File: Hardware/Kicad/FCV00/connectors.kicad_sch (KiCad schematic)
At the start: 24 parts, among them J2 ESC, J3 RX, J4 VTX, J5 CAM, J6 GPS, J7 AUX, Q1 2N7002

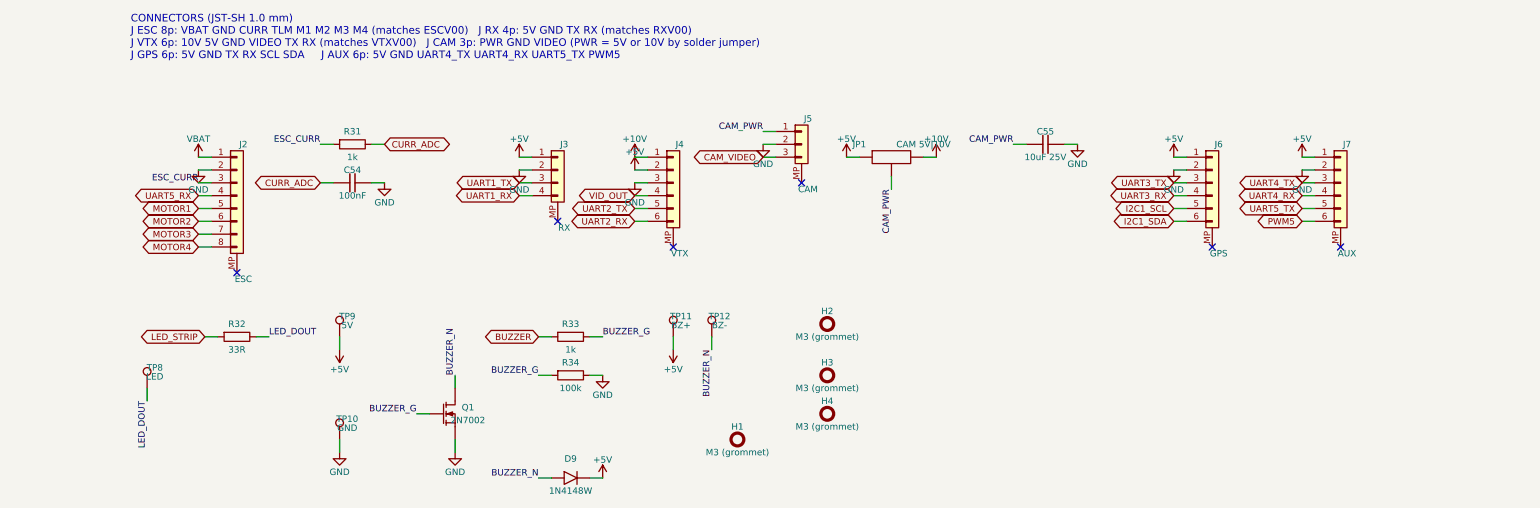
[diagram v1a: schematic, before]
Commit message: Boards follow the B0_EE part convention
- every real part uses the symbol/footprint/3D/datasheet named after its MPN in Kicad_Libs
- symbols keep only Reference, Value, Footprint, Datasheet, Description
  (MPN, Manufacturer, Verify, LCSC, Note fields removed; Verify notes moved to the Readme)
- schematic symbol caches rebuilt from the libraries, PCB footprints relinked with the
  same fields and 3D models as the library (connectivity unchanged)
- DNP and BOM attributes of the footprints match the symbols
- BOMs re-exported with kicad-cli
- ignore KiCad local history
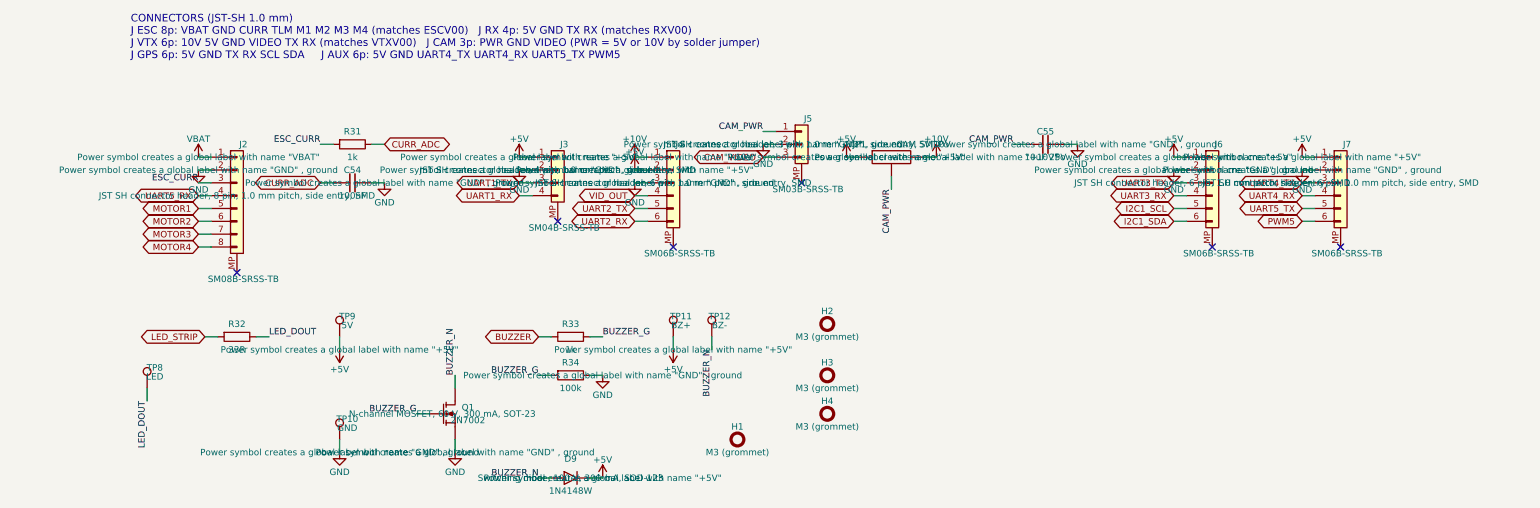
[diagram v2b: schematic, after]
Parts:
- D9: footprint eDiodes:D_SOD-123 -> eDiodes:1N4148W; symbol eDiodes:D -> eDiodes:1N4148W; MPN 1N4148W -> (none)
- H1, H2, H3, H4, JP1, TP10, TP11, TP12, TP8, TP9: now left out of the parts list
- J2: value ESC -> SM08B-SRSS-TB; footprint eConnector:JST_SH_SM08B-SRSS-TB_1x08-1MP_P1.00mm_Horizontal -> eConnector:SM08B-SRSS-TB; symbol eConnector:JST_SH_SM08B-SRSS-TB -> eConnector:SM08B-SRSS-TB; MPN SM08B-SRSS-TB(LF)(SN) -> (none); Manufacturer JST -> (none)
- J3: value RX -> SM04B-SRSS-TB; footprint eConnector:JST_SH_SM04B-SRSS-TB_1x04-1MP_P1.00mm_Horizontal -> eConnector:SM04B-SRSS-TB; symbol eConnector:JST_SH_SM04B-SRSS-TB -> eConnector:SM04B-SRSS-TB; MPN SM04B-SRSS-TB(LF)(SN) -> (none); Manufacturer JST -> (none)
- J4: value VTX -> SM06B-SRSS-TB; footprint eConnector:JST_SH_SM06B-SRSS-TB_1x06-1MP_P1.00mm_Horizontal -> eConnector:SM06B-SRSS-TB; symbol eConnector:JST_SH_SM06B-SRSS-TB -> eConnector:SM06B-SRSS-TB; MPN SM06B-SRSS-TB(LF)(SN) -> (none); Manufacturer JST -> (none)
- J5: value CAM -> SM03B-SRSS-TB; footprint eConnector:JST_SH_SM03B-SRSS-TB_1x03-1MP_P1.00mm_Horizontal -> eConnector:SM03B-SRSS-TB; symbol eConnector:JST_SH_SM03B-SRSS-TB -> eConnector:SM03B-SRSS-TB; MPN SM03B-SRSS-TB(LF)(SN) -> (none); Manufacturer JST -> (none)
- J6: value GPS -> SM06B-SRSS-TB; footprint eConnector:JST_SH_SM06B-SRSS-TB_1x06-1MP_P1.00mm_Horizontal -> eConnector:SM06B-SRSS-TB; symbol eConnector:JST_SH_SM06B-SRSS-TB -> eConnector:SM06B-SRSS-TB; MPN SM06B-SRSS-TB(LF)(SN) -> (none); Manufacturer JST -> (none)
- J7: value AUX -> SM06B-SRSS-TB; footprint eConnector:JST_SH_SM06B-SRSS-TB_1x06-1MP_P1.00mm_Horizontal -> eConnector:SM06B-SRSS-TB; symbol eConnector:JST_SH_SM06B-SRSS-TB -> eConnector:SM06B-SRSS-TB; MPN SM06B-SRSS-TB(LF)(SN) -> (none); Manufacturer JST -> (none)
- Q1: footprint eTransistor:SOT-23 -> eTransistor:2N7002; LCSC C8545 -> (none); MPN 2N7002,215 -> (none); Manufacturer Nexperia -> (none)

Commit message: Cleared all the descriptions and started Power section for FCV
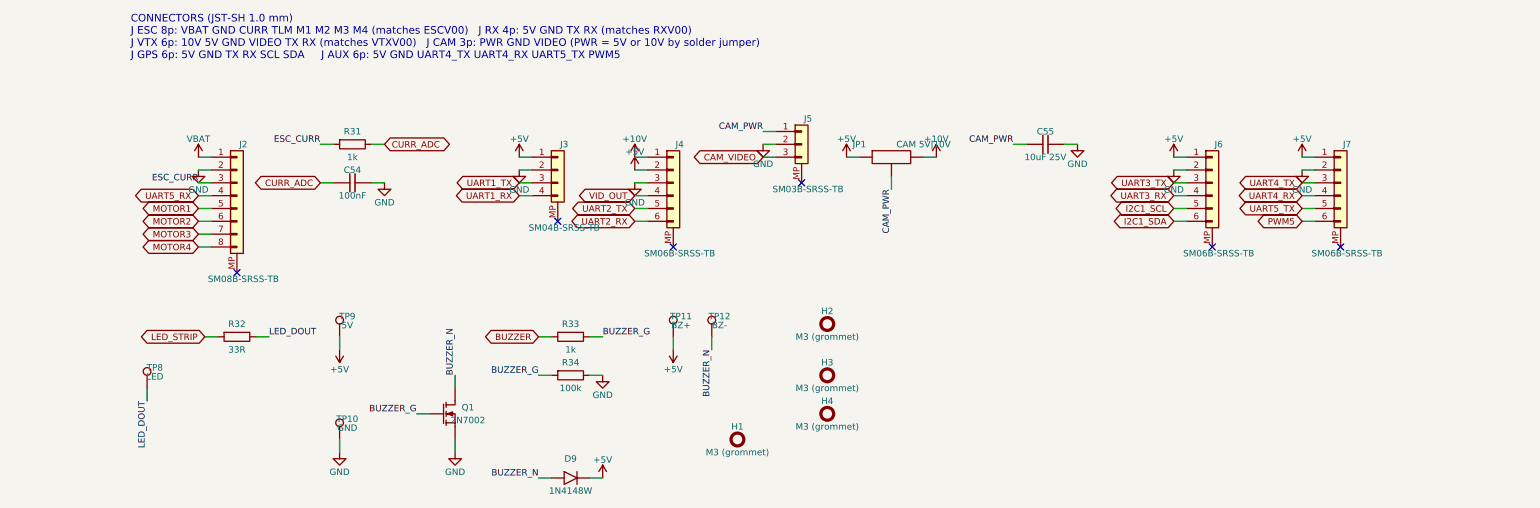
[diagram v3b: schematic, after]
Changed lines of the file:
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@@
 		(property "Description" "Power symbol creates a global label with name \"GND\" , ground"
 			(at 137.16 40.64 0)
+			(hide yes)
 			(show_name no)
 			(do_not_autoplace no)
@@
 		(property "Description" "Power symbol creates a global label with name \"GND\" , ground"
 			(at 111.76 48.26 0)
+			(hide yes)
 			(show_name no)
 			(do_not_autoplace no)
@@
 		(property "Description" "Power symbol creates a global label with name \"+5V\""
 			(at 111.76 45.72 0)
+			(hide yes)
 			(show_name no)
 			(do_not_autoplace no)
@@
 		(property "Description" "Power symbol creates a global label with name \"GND\" , ground"
 			(at 199.39 40.64 0)
+			(hide yes)
 			(show_name no)
 			(do_not_autoplace no)
@@
 		(property "Description" "JST SH connector header, 6 pin, 1.0 mm pitch, side entry, SMD"
 			(at 226.06 48.26 0)
+			(hide yes)
 			(show_name no)
 			(do_not_autoplace no)
@@
 		(property "Description" "Power symbol creates a global label with name \"+5V\""
 			(at 119.38 81.28 0)
+			(hide yes)
 			(show_name no)
 			(do_not_autoplace no)
@@
 		(property "Description" "Power symbol creates a global label with name \"+5V\""
 			(at 153.67 43.18 0)
+			(hide yes)
 			(show_name no)
 			(do_not_autoplace no)
@@
 		(property "Description" "Power symbol creates a global label with name \"+5V\""
 			(at 53.34 81.28 0)
+			(hide yes)
 			(show_name no)
 			(do_not_autoplace no)
@@
 		(property "Description" "Switching diode, 100 V, 300 mA, SOD-123"
 			(at 99.06 106.68 0)
+			(hide yes)
 			(show_name no)
 			(do_not_autoplace no)
@@
 		(property "Description" "Power symbol creates a global label with name \"+5V\""
 			(at 218.44 43.18 0)
+			(hide yes)
 			(show_name no)
 			(do_not_autoplace no)
@@
 		(property "Description" "JST SH connector header, 3 pin, 1.0 mm pitch, side entry, SMD"
 			(at 144.78 40.64 0)
+			(hide yes)
 			(show_name no)
 			(do_not_autoplace no)
@@
 		(property "Description" "Power symbol creates a global label with name \"GND\" , ground"
 			(at 76.2 101.6 0)
+			(hide yes)
 			(show_name no)
 			(do_not_autoplace no)
@@
 		(property "Description" "Power symbol creates a global label with name \"+5V\""
 			(at 88.9 43.18 0)
+			(hide yes)
 			(show_name no)
 			(do_not_autoplace no)
@@
 		(property "Description" "Power symbol creates a global label with name \"+5V\""
 			(at 105.41 106.68 0)
+			(hide yes)
 			(show_name no)
 			(do_not_autoplace no)
@@
 		(property "Description" "Power symbol creates a global label with name \"GND\" , ground"
 			(at 62.23 48.26 0)
+			(hide yes)
 			(show_name no)
 			(do_not_autoplace no)
@@
 		(property "Description" "Power symbol creates a global label with name \"VBAT\""
 			(at 25.4 43.18 0)
+			(hide yes)
 			(show_name no)
 			(do_not_autoplace no)
@@
 		(property "Description" "Power symbol creates a global label with name \"GND\" , ground"
 			(at 105.41 86.36 0)
+			(hide yes)
 			(show_name no)
 			(do_not_autoplace no)
@@
 		(property "Description" "Power symbol creates a global label with name \"+10V\""
 			(at 171.45 43.18 0)
+			(hide yes)
 			(show_name no)
 			(do_not_autoplace no)
@@
 		(property "Description" "JST SH connector header, 4 pin, 1.0 mm pitch, side entry, SMD"
 			(at 96.52 45.72 0)
+			(hide yes)
 			(show_name no)
 			(do_not_autoplace no)
@@
 		(property "Description" "Power symbol creates a global label with name \"+10V\""
 			(at 111.76 43.18 0)
+			(hide yes)
 			(show_name no)
 			(do_not_autoplace no)
@@
 		(property "Description" "Power symbol creates a global label with name \"+5V\""
 			(at 243.84 43.18 0)
+			(hide yes)
 			(show_name no)
 			(do_not_autoplace no)
@@
 		(property "Description" "Power symbol creates a global label with name \"GND\" , ground"
 			(at 88.9 45.72 0)
+			(hide yes)
 			(show_name no)
 			(do_not_autoplace no)
@@
 		(property "Description" "JST SH connector header, 6 pin, 1.0 mm pitch, side entry, SMD"
 			(at 251.46 48.26 0)
+			(hide yes)
 			(show_name no)
 			(do_not_autoplace no)
@@
 		(property "Description" "JST SH connector header, 6 pin, 1.0 mm pitch, side entry, SMD"
 			(at 119.38 48.26 0)
+			(hide yes)
 			(show_name no)
 			(do_not_autoplace no)
@@
 		(property "Description" "Power symbol creates a global label with name \"GND\" , ground"
 			(at 218.44 45.72 0)
+			(hide yes)
 			(show_name no)
 			(do_not_autoplace no)
@@
 		(property "Description" "N-channel MOSFET, 60 V, 300 mA, SOT-23"
 			(at 73.66 93.98 0)
+			(hide yes)
 			(show_name no)
 			(do_not_autoplace no)
@@
 		(property "Description" "JST SH connector header, 8 pin, 1.0 mm pitch, side entry, SMD"
 			(at 33.02 50.8 0)
+			(hide yes)
 			(show_name no)
 			(do_not_autoplace no)
@@
 		(property "Description" "Power symbol creates a global label with name \"GND\" , ground"
 			(at 53.34 101.6 0)
+			(hide yes)
 			(show_name no)
 			(do_not_autoplace no)
@@
 		(property "Description" "Power symbol creates a global label with name \"GND\" , ground"
 			(at 25.4 45.72 0)
+			(hide yes)
 			(show_name no)
 			(do_not_autoplace no)
@@
 		(property "Description" "Power symbol creates a global label with name \"GND\" , ground"
 			(at 243.84 45.72 0)
+			(hide yes)
 			(show_name no)
 			(do_not_autoplace no)
